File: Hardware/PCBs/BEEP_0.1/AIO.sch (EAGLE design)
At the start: 70 parts, among them IC1 ULN2803ASOP18, IC2 ULN2803ASOP18, IC3 74HC238D, IC4 74HC238D, U2 TB6612FNG, U3 ATXMEGA64D3-AU, X1 MICROMATCH-8, X10 MICROMATCH-10, X2 MICROMATCH-8, X3 MICROMATCH-8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

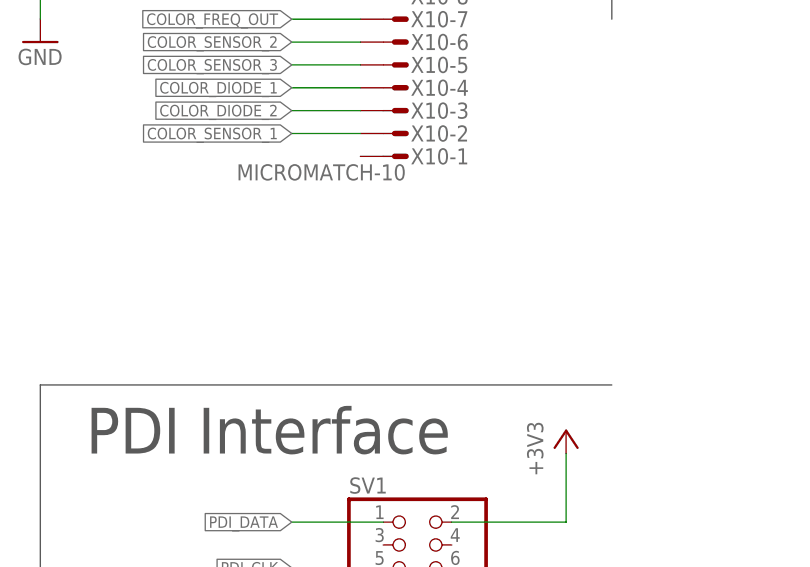
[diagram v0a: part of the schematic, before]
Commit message: *add i2c connector *continue routing
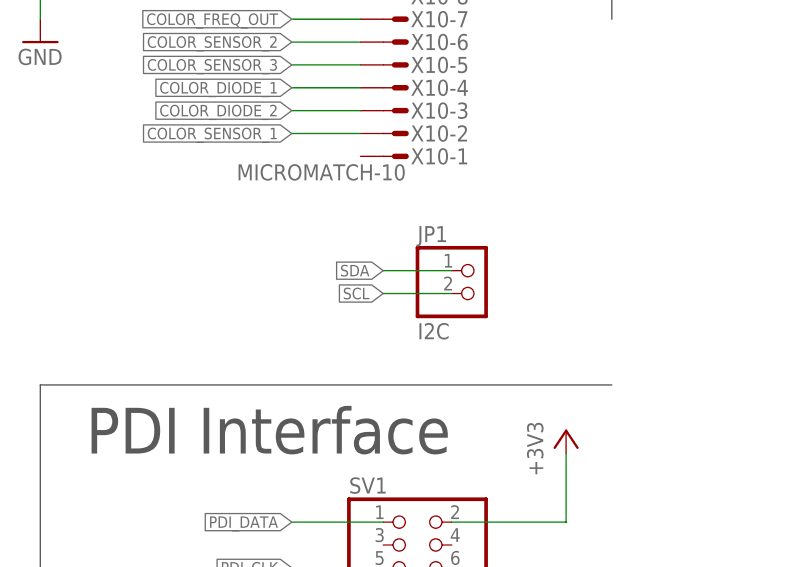
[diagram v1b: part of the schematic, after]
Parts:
- added JP1: I2C, pinhead:PINHD-1X2
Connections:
- net SCL: now also JP1.2
- net SDA: now also JP1.1
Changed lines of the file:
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@@
 <part name="C12" library="rcl" deviceset="C-EU" device="C0603" value="100nF"/>
 <part name="U3" library="atmel-xmega" deviceset="ATXMEGA64D3" device="-AU"/>
+<part name="JP1" library="pinhead" deviceset="PINHD-1X2" device="" value="I2C"/>
 </parts>
 <sheets>
@@
 <instance part="C12" gate="G$1" x="38.1" y="363.22" rot="R180"/>
 <instance part="U3" gate="G$1" x="111.76" y="116.84"/>
+<instance part="JP1" gate="G$1" x="254" y="93.98"/>
 </instances>
 <busses>
@@
 <label x="88.9" y="111.76" size="1.27" layer="95" rot="R180" xref="yes"/>
 </segment>
+<segment>
+<pinref part="JP1" gate="G$1" pin="2"/>
+<wire x1="251.46" y1="93.98" x2="243.84" y2="93.98" width="0.1524" layer="91"/>
+<label x="243.84" y="93.98" size="1.27" layer="95" rot="R180" xref="yes"/>
+</segment>
 </net>
 <net name="SDA" class="0">
@@
 <label x="88.9" y="114.3" size="1.27" layer="95" rot="R180" xref="yes"/>
 </segment>
-</net>
+<segment>
+<pinref part="JP1" gate="G$1" pin="1"/>
+<wire x1="251.46" y1="96.52" x2="243.84" y2="96.52" width="0.1524" layer="91"/>
+<label x="243.84" y="96.52" size="1.27" layer="95" rot="R180" xref="yes"/>
+</segment>
+</net>

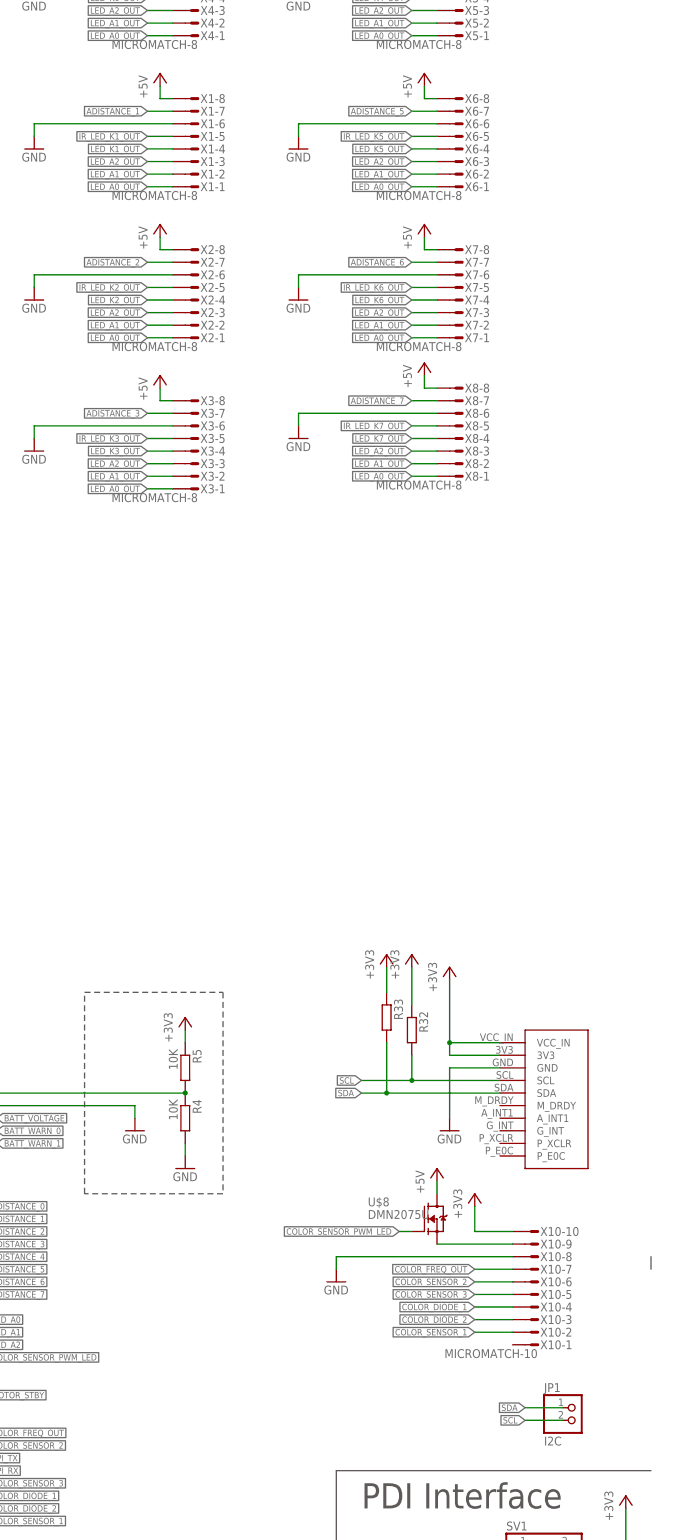
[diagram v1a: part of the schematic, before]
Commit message: add i2c header continue routing
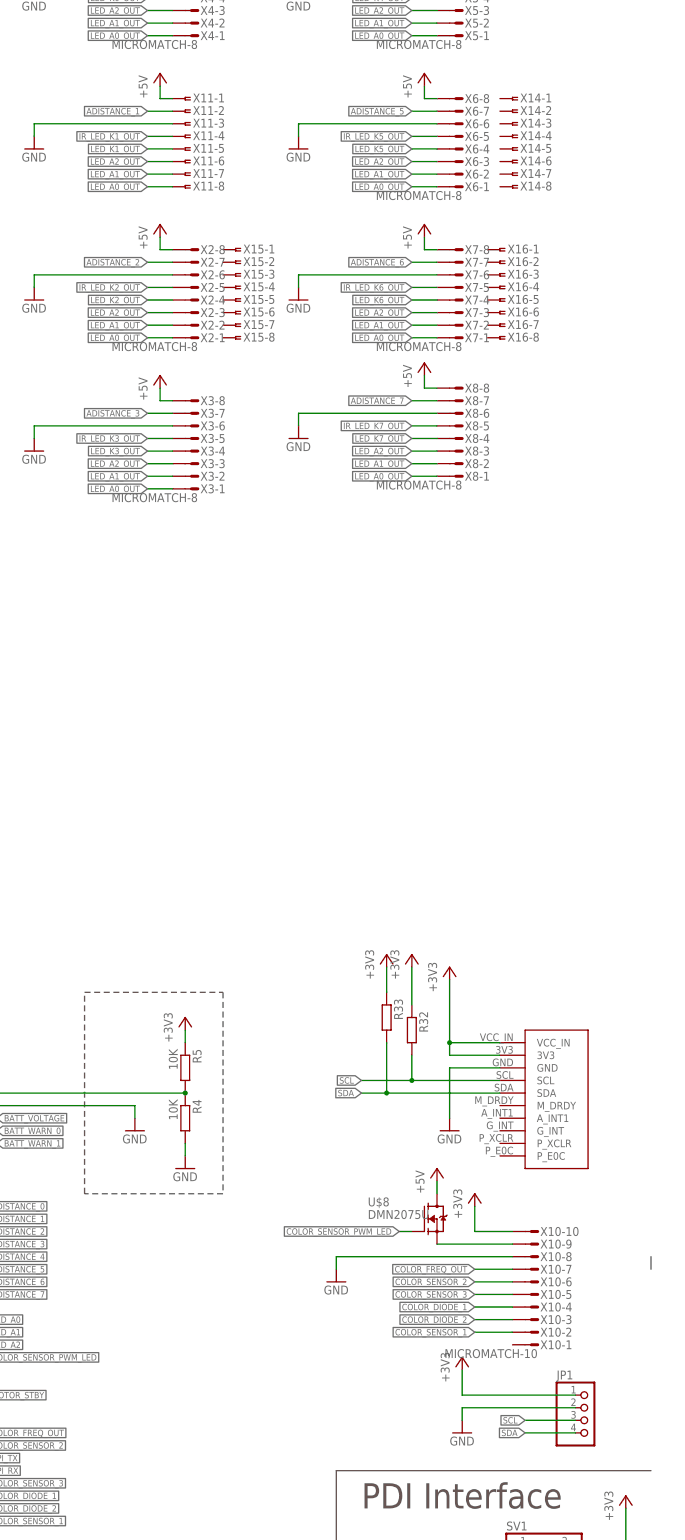
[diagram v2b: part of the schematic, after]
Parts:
- removed X1: MICROMATCH-8, Con-amp-micromatch:MICROMATCH-8
- added X11, X14, X15, X16: (no value), con-amp:FSIDE-8
- JP1: value I2C -> (none); device pinhead:PINHD-1X2 -> pinhead:PINHD-1X4
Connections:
- net +3V3: now also JP1.1
- net +5V: now also X11-1.1; no longer X1-8.S
- net ADISTANCE_1: now also X11-2.1; no longer X1-7.S
- net GND: now also JP1.2, X11-3.1; no longer X1-6.S
- net IR_LED_K1_OUT: now also X11-4.1; no longer X1-5.S
- net LED_A0_OUT: now also X11-8.1; no longer X1-1.S
- net LED_A1_OUT: now also X11-7.1; no longer X1-2.S
- net LED_A2_OUT: now also X11-6.1; no longer X1-3.S
- net LED_K1_OUT: now also X11-5.1; no longer X1-4.S
- net SCL: now also JP1.3; no longer JP1.2
- net SDA: now also JP1.4; no longer JP1.1
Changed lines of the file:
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@@
 <part name="GND2" library="supply1" deviceset="GND" device=""/>
 <part name="P+4" library="supply1" deviceset="+5V" device=""/>
-<part name="X1" library="Con-amp-micromatch" deviceset="MICROMATCH-8" device=""/>
 <part name="GND6" library="supply1" deviceset="GND" device=""/>
 <part name="P+5" library="supply1" deviceset="+5V" device=""/>
@@
 <part name="C12" library="rcl" deviceset="C-EU" device="C0603" value="100nF"/>
 <part name="U3" library="atmel-xmega" deviceset="ATXMEGA64D3" device="-AU"/>
-<part name="JP1" library="pinhead" deviceset="PINHD-1X2" device="" value="I2C"/>
+<part name="+3V7" library="supply1" deviceset="+3V3" device=""/>
+<part name="GND5" library="supply1" deviceset="GND" device=""/>
+<part name="JP1" library="pinhead" deviceset="PINHD-1X4" device=""/>
+<part name="X11" library="con-amp" deviceset="FSIDE-8" device=""/>
+<part name="X14" library="con-amp" deviceset="FSIDE-8" device=""/>
+<part name="X15" library="con-amp" deviceset="FSIDE-8" device=""/>
+<part name="X16" library="con-amp" deviceset="FSIDE-8" device=""/>
 </parts>
 <sheets>
@@
 <instance part="GND2" gate="1" x="78.74" y="276.86"/>
 <instance part="P+4" gate="1" x="170.18" y="396.24"/>
-<instance part="X1" gate="-1" x="177.8" y="342.9" rot="R180"/>
-<instance part="X1" gate="-2" x="177.8" y="345.44" rot="R180"/>
-<instance part="X1" gate="-3" x="177.8" y="347.98" rot="R180"/>
-<instance part="X1" gate="-4" x="177.8" y="350.52" rot="R180"/>
-<instance part="X1" gate="-5" x="177.8" y="353.06" rot="R180"/>
-<instance part="X1" gate="-6" x="177.8" y="355.6" rot="R180"/>
-<instance part="X1" gate="-7" x="177.8" y="358.14" rot="R180"/>
-<instance part="X1" gate="-8" x="177.8" y="360.68" rot="R180"/>
 <instance part="GND6" gate="1" x="144.78" y="350.52"/>
 <instance part="P+5" gate="1" x="170.18" y="365.76"/>
@@
 <instance part="C12" gate="G$1" x="38.1" y="363.22" rot="R180"/>
 <instance part="U3" gate="G$1" x="111.76" y="116.84"/>
-<instance part="JP1" gate="G$1" x="254" y="93.98"/>
+<instance part="+3V7" gate="G$1" x="231.14" y="106.68"/>
+<instance part="GND5" gate="1" x="231.14" y="91.44"/>
+<instance part="JP1" gate="A" x="256.54" y="93.98"/>
+<instance part="X11" gate="-1" x="175.26" y="360.68"/>
+<instance part="X11" gate="-2" x="175.26" y="358.14"/>
+<instance part="X11" gate="-3" x="175.26" y="355.6"/>
+<instance part="X11" gate="-4" x="175.26" y="353.06"/>
+<instance part="X11" gate="-5" x="175.26" y="350.52"/>
+<instance part="X11" gate="-6" x="175.26" y="347.98"/>
+<instance part="X11" gate="-7" x="175.26" y="345.44"/>
+<instance part="X11" gate="-8" x="175.26" y="342.9"/>
+<instance part="X14" gate="-1" x="241.3" y="360.68"/>
+<instance part="X14" gate="-2" x="241.3" y="358.14"/>
+<instance part="X14" gate="-3" x="241.3" y="355.6"/>
+<instance part="X14" gate="-4" x="241.3" y="353.06"/>
+<instance part="X14" gate="-5" x="241.3" y="350.52"/>
+<instance part="X14" gate="-6" x="241.3" y="347.98"/>
+<instance part="X14" gate="-7" x="241.3" y="345.44"/>
+<instance part="X14" gate="-8" x="241.3" y="342.9"/>
+<instance part="X15" gate="-1" x="185.42" y="330.2"/>
+<instance part="X15" gate="-2" x="185.42" y="327.66"/>
+<instance part="X15" gate="-3" x="185.42" y="325.12"/>
+<instance part="X15" gate="-4" x="185.42" y="322.58"/>
+<instance part="X15" gate="-5" x="185.42" y="320.04"/>
+<instance part="X15" gate="-6" x="185.42" y="317.5"/>
+<instance part="X15" gate="-7" x="185.42" y="314.96"/>
+<instance part="X15" gate="-8" x="185.42" y="312.42"/>
+<instance part="X16" gate="-1" x="238.76" y="330.2"/>
+<instance part="X16" gate="-2" x="238.76" y="327.66"/>
+<instance part="X16" gate="-3" x="238.76" y="325.12"/>
+<instance part="X16" gate="-4" x="238.76" y="322.58"/>
+<instance part="X16" gate="-5" x="238.76" y="320.04"/>
+<instance part="X16" gate="-6" x="238.76" y="317.5"/>
+<instance part="X16" gate="-7" x="238.76" y="314.96"/>
+<instance part="X16" gate="-8" x="238.76" y="312.42"/>
 </instances>
 <busses>
@@
 <pinref part="GND6" gate="1" pin="GND"/>
 <wire x1="144.78" y1="353.06" x2="144.78" y2="355.6" width="0.1524" layer="91"/>
-<pinref part="X1" gate="-6" pin="S"/>
 <wire x1="172.72" y1="355.6" x2="144.78" y2="355.6" width="0.1524" layer="91"/>
+<pinref part="X11" gate="-3" pin="1"/>
 </segment>
 <segment>
@@
 <wire x1="353.06" y1="347.98" x2="353.06" y2="355.6" width="0.1524" layer="91"/>
 </segment>
+<segment>
+<pinref part="JP1" gate="A" pin="2"/>
+<pinref part="GND5" gate="1" pin="GND"/>
+<wire x1="254" y1="96.52" x2="231.14" y2="96.52" width="0.1524" layer="91"/>
+<wire x1="231.14" y1="96.52" x2="231.14" y2="93.98" width="0.1524" layer="91"/>
+</segment>
 </net>
 <net name="+5V" class="0">
@@
 </segment>
 <segment>
-<pinref part="X1" gate="-8" pin="S"/>
 <wire x1="172.72" y1="360.68" x2="170.18" y2="360.68" width="0.1524" layer="91"/>
 <wire x1="170.18" y1="360.68" x2="170.18" y2="363.22" width="0.1524" layer="91"/>
 <pinref part="P+5" gate="1" pin="+5V"/>
+<pinref part="X11" gate="-1" pin="1"/>
 </segment>
 <segment>
@@
 <wire x1="22.86" y1="340.36" x2="22.86" y2="350.52" width="0.1524" layer="91"/>
 </segment>
+<segment>
+<pinref part="JP1" gate="A" pin="1"/>
+<pinref part="+3V7" gate="G$1" pin="+3V3"/>
+<wire x1="254" y1="99.06" x2="231.14" y2="99.06" width="0.1524" layer="91"/>
+<wire x1="231.14" y1="99.06" x2="231.14" y2="104.14" width="0.1524" layer="91"/>
+</segment>
 </net>
 <net name="MOTOR_B_PWM" class="0">
@@
 </segment>
 <segment>
-<pinref part="JP1" gate="G$1" pin="2"/>
-<wire x1="251.46" y1="93.98" x2="243.84" y2="93.98" width="0.1524" layer="91"/>
+<wire x1="254" y1="93.98" x2="243.84" y2="93.98" width="0.1524" layer="91"/>
 <label x="243.84" y="93.98" size="1.27" layer="95" rot="R180" xref="yes"/>
+<pinref part="JP1" gate="A" pin="3"/>
 </segment>
 </net>
@@
 </segment>
 <segment>
-<pinref part="JP1" gate="G$1" pin="1"/>
-<wire x1="251.46" y1="96.52" x2="243.84" y2="96.52" width="0.1524" layer="91"/>
-<label x="243.84" y="96.52" size="1.27" layer="95" rot="R180" xref="yes"/>
+<wire x1="254" y1="91.44" x2="243.84" y2="91.44" width="0.1524" layer="91"/>
+<label x="243.84" y="91.44" size="1.27" layer="95" rot="R180" xref="yes"/>
+<pinref part="JP1" gate="A" pin="4"/>
 </segment>
 </net>
@@
 </segment>
 <segment>
-<pinref part="X1" gate="-4" pin="S"/>
 <wire x1="172.72" y1="350.52" x2="167.64" y2="350.52" width="0.1524" layer="91"/>
 <label x="167.64" y="350.52" size="1.27" layer="95" rot="R180" xref="yes"/>
+<pinref part="X11" gate="-5" pin="1"/>
 </segment>
 </net>
@@
 </segment>
 <segment>
-<pinref part="X1" gate="-3" pin="S"/>
 <wire x1="172.72" y1="347.98" x2="167.64" y2="347.98" width="0.1524" layer="91"/>
 <label x="167.64" y="347.98" size="1.27" layer="95" rot="R180" xref="yes"/>
+<pinref part="X11" gate="-6" pin="1"/>
 </segment>
 <segment>
@@
 </segment>
 <segment>
-<pinref part="X1" gate="-2" pin="S"/>
 <wire x1="172.72" y1="345.44" x2="167.64" y2="345.44" width="0.1524" layer="91"/>
 <label x="167.64" y="345.44" size="1.27" layer="95" rot="R180" xref="yes"/>
+<pinref part="X11" gate="-7" pin="1"/>
 </segment>
 <segment>
@@
 </segment>
 <segment>
-<pinref part="X1" gate="-1" pin="S"/>
 <wire x1="172.72" y1="342.9" x2="167.64" y2="342.9" width="0.1524" layer="91"/>
 <label x="167.64" y="342.9" size="1.27" layer="95" rot="R180" xref="yes"/>
+<pinref part="X11" gate="-8" pin="1"/>
 </segment>
 <segment>
@@
 </segment>
 <segment>
-<pinref part="X1" gate="-5" pin="S"/>
 <wire x1="172.72" y1="353.06" x2="167.64" y2="353.06" width="0.1524" layer="91"/>
 <label x="167.64" y="353.06" size="1.27" layer="95" rot="R180" xref="yes"/>
+<pinref part="X11" gate="-4" pin="1"/>
 </segment>
 </net>
@@
 <net name="ADISTANCE_1" class="0">
 <segment>
-<pinref part="X1" gate="-7" pin="S"/>
 <wire x1="172.72" y1="358.14" x2="167.64" y2="358.14" width="0.1524" layer="91"/>
 <label x="167.64" y="358.14" size="1.27" layer="95" rot="R180" xref="yes"/>
-</segment>
-<segment>
+<pinref part="X11" gate="-2" pin="1"/>
+</segment>
+<segment>
